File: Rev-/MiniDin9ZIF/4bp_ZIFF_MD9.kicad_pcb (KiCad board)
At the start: 2 copper layers, 38.8 x 60.7 mm, 132 parts, among them CN1 MD-90SM_MD2, IC1 THS7374IPWR, IC2 TL974, IC3 AD724, J1 SMD_Conn_01x01, J2 SMD_Conn_01x01, J3 SolderJumper_2_Open, J4 SMD_Conn_01x01, J5 SMD_Conn_01x01, M1PU1 SolderJumper_2_Open, P1 SMD_Conn_01x01

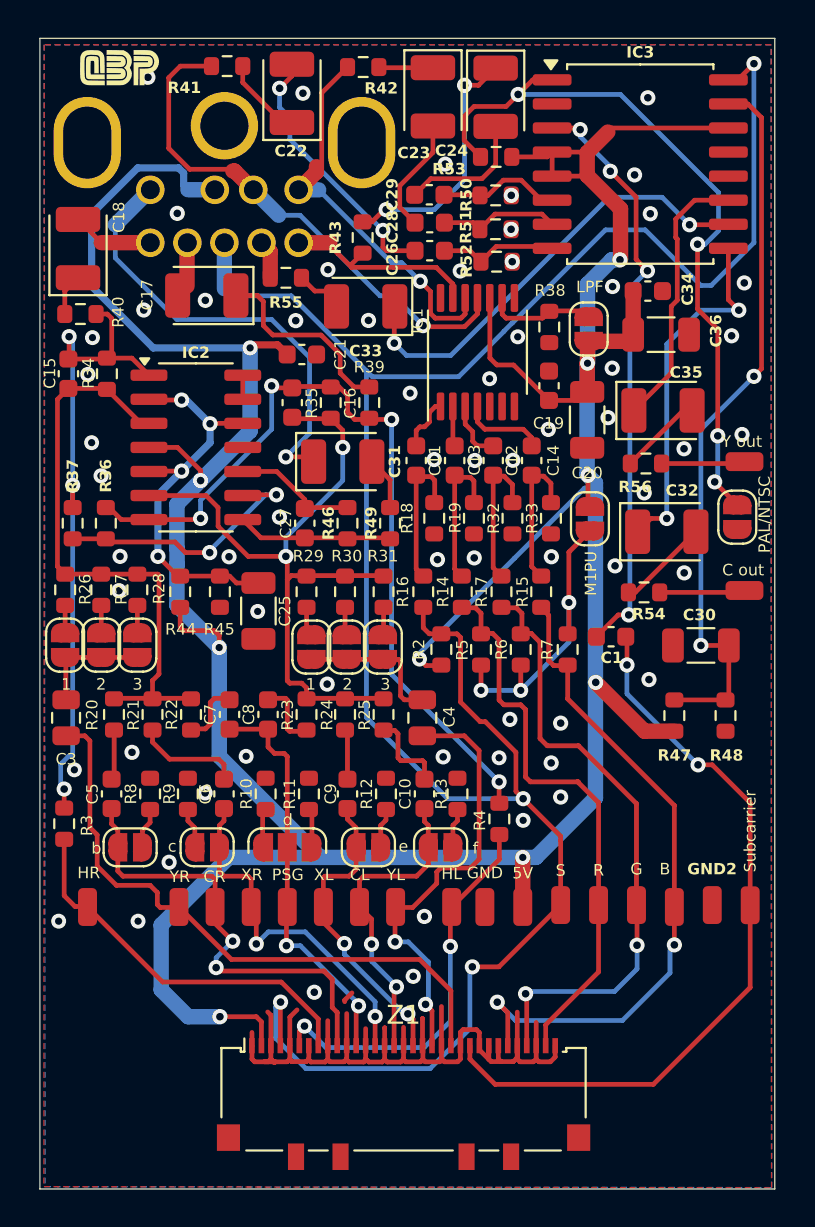
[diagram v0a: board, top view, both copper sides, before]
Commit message: fix drc
connect 2 capacitors to GND
adjust netclass clearance
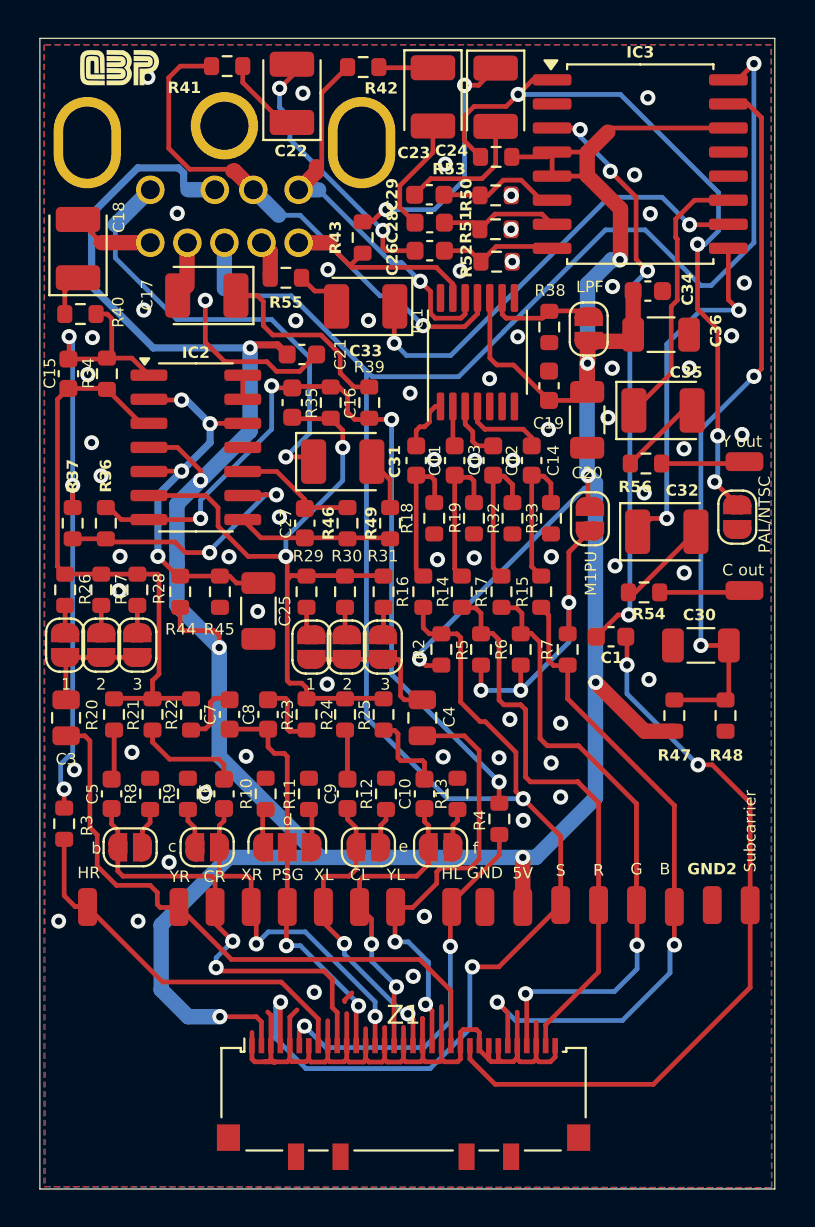
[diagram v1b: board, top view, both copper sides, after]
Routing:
- net GND: track 50.7 -> 59.5 mm, vias 64 -> 65
- net /CR: track 24.2 -> 23.3 mm
- net /XL: track 16.3 -> 15.4 mm
- net +5V: track 191.8 -> 191.0 mm
- net Net-(IC2C--): track 14.5 -> 13.9 mm
- net Net-(IC3-RIN): track 6.49 -> 5.87 mm
- net Net-(IC3-BIN): track 6.68 -> 6.16 mm
